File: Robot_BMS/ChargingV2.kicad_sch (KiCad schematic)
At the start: 11 parts, among them Q1 2N7002, U1 TPS54308DDCR

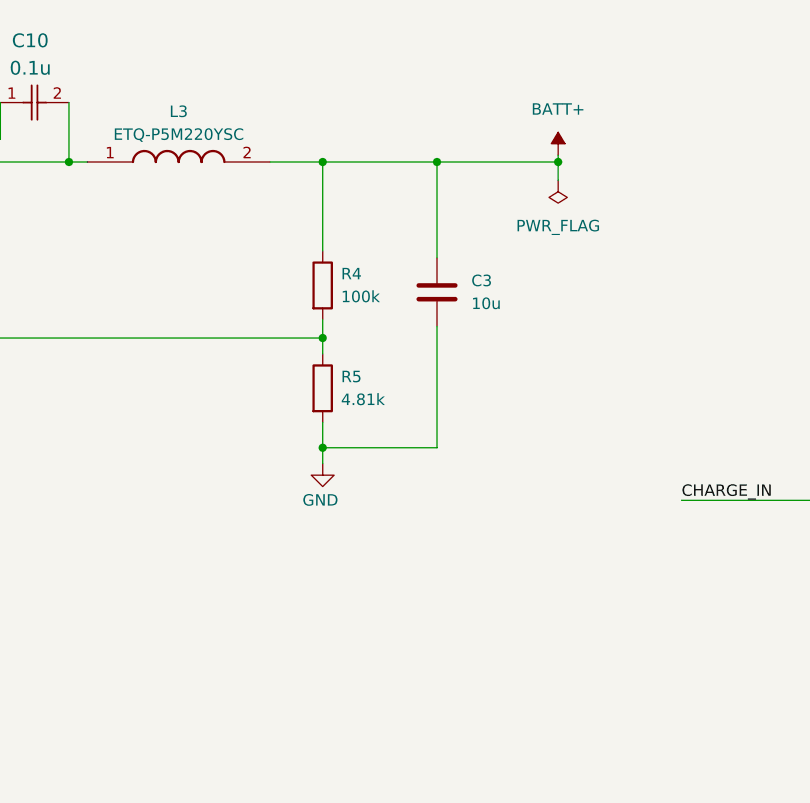
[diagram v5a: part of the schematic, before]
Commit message: still adding in symbols & footprints for passives
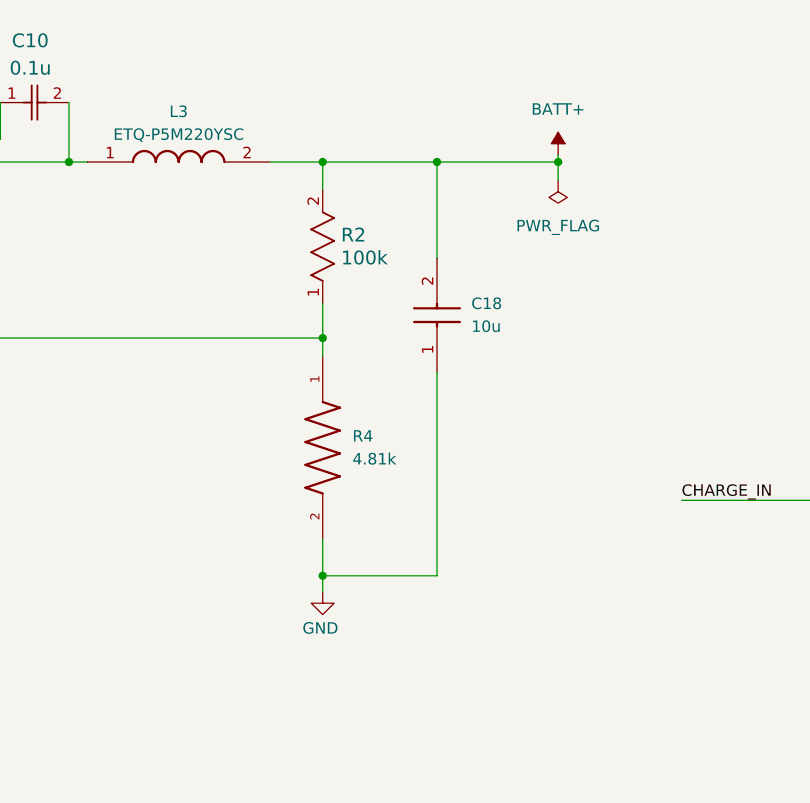
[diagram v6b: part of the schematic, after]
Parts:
- removed C3: 10u, symbol Device:C
- removed R4: 100k, symbol Device:R
- removed R5: 4.81k, symbol Device:R
- added C18: 10u, CAPC1608X90N, symbol CL10A106MA8NRNC:CL10A106MA8NRNC
- added R2: 100k, RES_R0603_ROM, symbol ESR03EZPF1003:ESR03EZPF1003
- added R4: 4.81k, RN73H1JTTD4811B25:RESC1608X55N, symbol RN73H1JTTD4811B25:RN73H1JTTD4811B25
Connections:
- net BATT+: now also C18.2, R2.2
- net GND: now also C18.1, R4.2
- net at U1.4 (FB): now also R2.1, R4.1

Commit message: all symbols footprints & models added
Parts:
- C2: renamed from C10; footprint CAPC17595_87N_KEM -> RobotBMS:CAPC17595_87N_KEM
- C3: renamed from C18; footprint CAPC1608X90N -> RobotBMS:CAPC1608X90N
- L1: renamed from L3; footprint ETQP5M220YSC -> RobotBMS:ETQP5M220YSC
- R4: renamed from R2; footprint RES_R0603_ROM -> RobotBMS:RES_R0603_ROM
- R5: renamed from R4; footprint RN73H1JTTD4811B25:RESC1608X55N -> RobotBMS:RESC1608X55N
- renumbered C24 to C1
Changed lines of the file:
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@@
 		(dnp no)
 		(fields_autoplaced yes)
-		(property "Reference" "L3"
+		(property "Reference" "L1"
 			(at 121.412 65.024 0)
 			(effects
@@
 			)
 		)
-		(property "Footprint" "ETQP5M220YSC"
+		(property "Footprint" "RobotBMS:ETQP5M220YSC"
 			(at 127.762 166.802 0)
 			(effects
@@
 			(project ""
 				(path "/72551b1c-3d40-4199-8911-e5b015f4abec/31837631-dd5f-49d4-a8ae-a36c80dc2ea1"
-					(reference "L3")
+					(reference "L1")
 					(unit 1)
 				)
@@
 		(dnp no)
 		(fields_autoplaced yes)
-		(property "Reference" "R2"
+		(property "Reference" "R4"
 			(at 139.446 78.7399 90)
 			(effects
@@
 			)
 		)
-		(property "Footprint" "RES_R0603_ROM"
+		(property "Footprint" "RobotBMS:RES_R0603_ROM"
 			(at 137.414 86.36 0)
 			(effects
@@
 			(project ""
 				(path "/72551b1c-3d40-4199-8911-e5b015f4abec/31837631-dd5f-49d4-a8ae-a36c80dc2ea1"
-					(reference "R2")
+					(reference "R4")
 					(unit 1)
 				)
@@
 		(dnp no)
 		(fields_autoplaced yes)
-		(property "Reference" "C18"
+		(property "Reference" "C3"
 			(at 153.924 86.3599 90)
 			(effects
@@
 			)
 		)
-		(property "Footprint" "CAPC1608X90N"
+		(property "Footprint" "RobotBMS:CAPC1608X90N"
 			(at 246.304 85.09 0)
 			(effects
@@
 			(project ""
 				(path "/72551b1c-3d40-4199-8911-e5b015f4abec/31837631-dd5f-49d4-a8ae-a36c80dc2ea1"
-					(reference "C18")
+					(reference "C3")
 					(unit 1)
 				)
@@
 		(on_board yes)
 		(dnp no)
-		(property "Reference" "C10"
+		(property "Reference" "C2"
 			(at 102.87 57.15 0)
 			(effects
@@
 			)
 		)
-		(property "Footprint" "CAPC17595_87N_KEM"
+		(property "Footprint" "RobotBMS:CAPC17595_87N_KEM"
 			(at 101.6 64.008 0)
 			(effects
@@
 			(project "Robot_BMS"
 				(path "/72551b1c-3d40-4199-8911-e5b015f4abec/31837631-dd5f-49d4-a8ae-a36c80dc2ea1"
-					(reference "C10")
+					(reference "C2")
 					(unit 1)
 				)
@@
 		(on_board yes)
 		(dnp no)
-		(property "Reference" "C24"
+		(property "Reference" "C1"
 			(at 36.576 73.6599 90)
 			(effects
@@
 			(project ""
 				(path "/72551b1c-3d40-4199-8911-e5b015f4abec/31837631-dd5f-49d4-a8ae-a36c80dc2ea1"
-					(reference "C24")
+					(reference "C1")
 					(unit 1)
 				)
@@
 		(dnp no)
 		(fields_autoplaced yes)
-		(property "Reference" "R4"
+		(property "Reference" "R5"
 			(at 140.716 101.0919 90)
 			(effects
@@
 			)
 		)
-		(property "Footprint" "RN73H1JTTD4811B25:RESC1608X55N"
+		(property "Footprint" "RobotBMS:RESC1608X55N"
 			(at 137.414 102.362 0)
 			(effects
@@
 			(project ""
 				(path "/72551b1c-3d40-4199-8911-e5b015f4abec/31837631-dd5f-49d4-a8ae-a36c80dc2ea1"
-					(reference "R4")
-					(unit 1)
-				)
+					(reference "R5")
+					(unit 1)
+				)

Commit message: BOM done, with total price £40
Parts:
- C1: Manufacturer_Part_Number (none) -> GRM188R61H225KE11D; Price (none) -> 0.22
- C2: Manufacturer_Part_Number (none) -> C0603C104K5RACAUTO; Price (none) -> 0.05
- C3: Price (none) -> 0.11
- CR1, CR2, CR3: Manufacturer_Part_Number (none) -> CMS05TE12L_Q_M; Price (none) -> 0.80
- L1: Price (none) -> 1.20
- Q1: Manufacturer_Part_Number (none) -> 2N7002 H6327; Price (none) -> 0.21
- R4: Manufacturer_Part_Number (none) -> ESR03EZPF1003; Price (none) -> 0.12
- R5: Manufacturer_Part_Number (none) -> RN73H1JTTD4811B25; Price (none) -> 0.18
- U1: Manufacturer_Part_Number (none) -> TPS54308DDCR; Price (none) -> 1.10
